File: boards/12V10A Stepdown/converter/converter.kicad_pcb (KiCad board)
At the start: 4 copper layers, 64 x 48 mm, 31 parts, among them J1 TB005-762-02BE, J2 TB005-762-02BE, M1 CSD17578Q3A, M2 CSD17571Q2, U1 LM25145RGYR

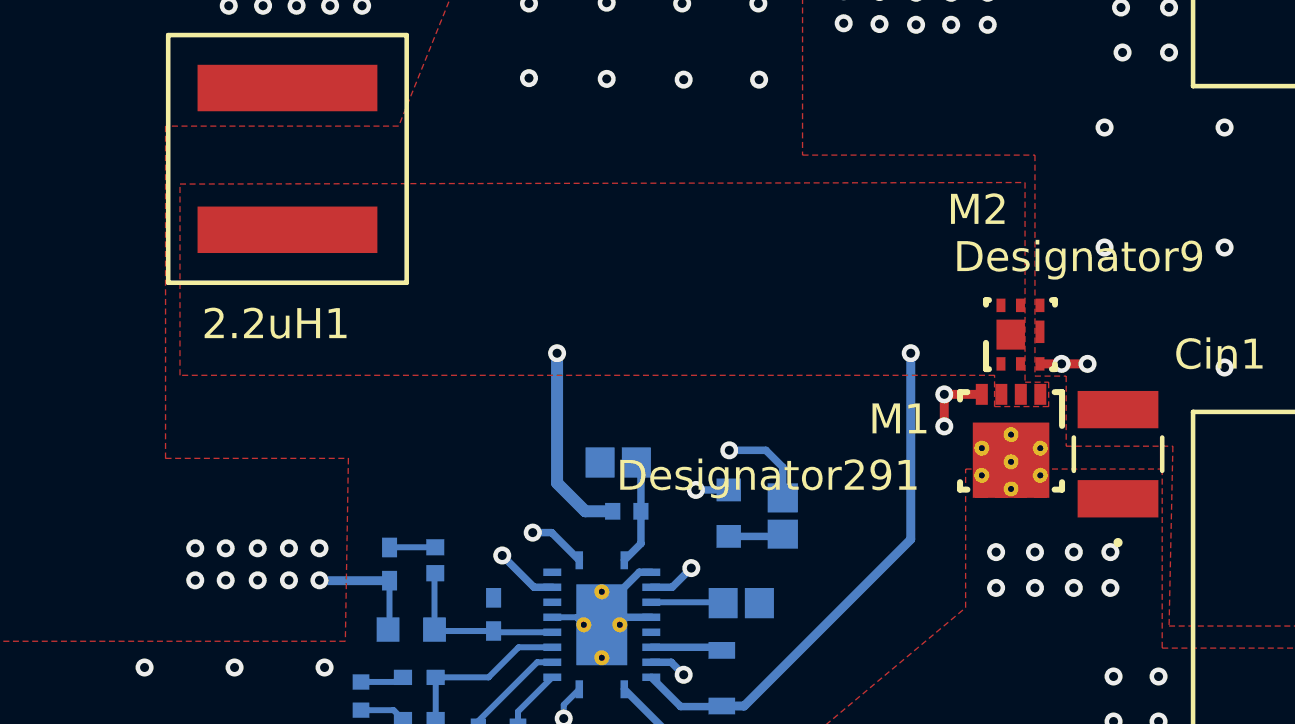
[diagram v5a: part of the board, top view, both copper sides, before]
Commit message: removed backfill on 20a
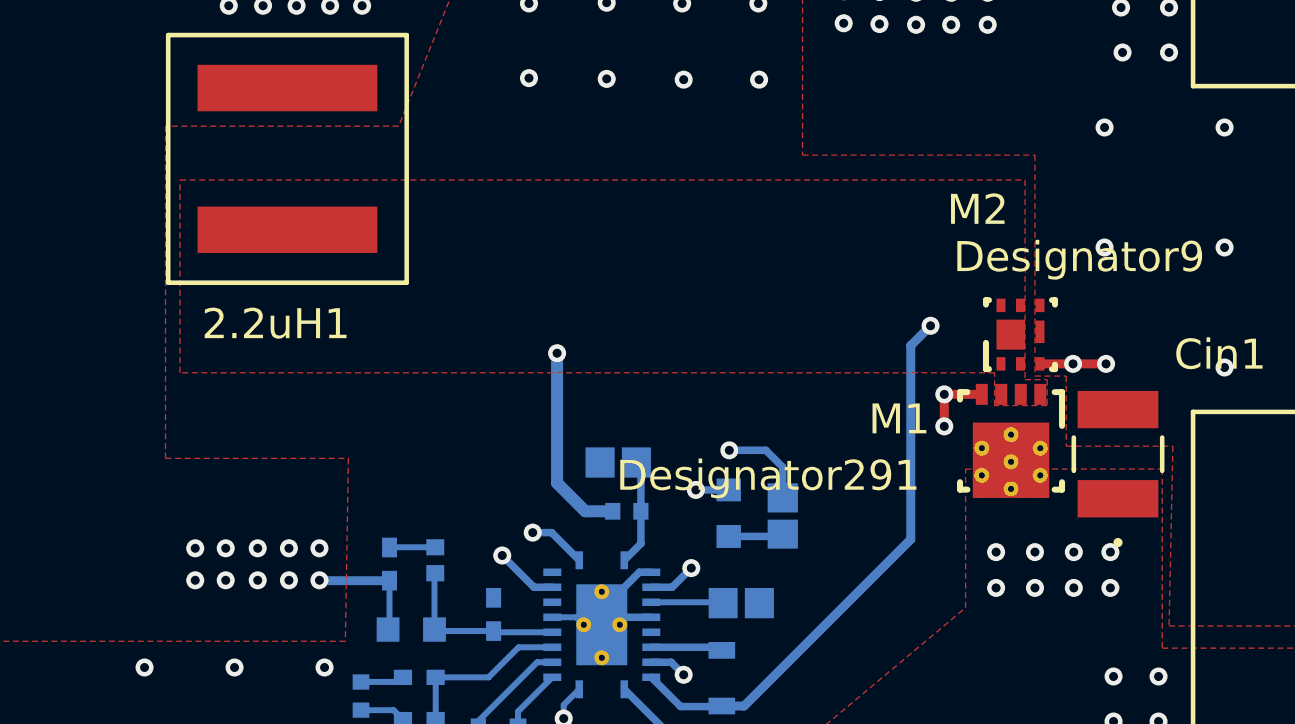
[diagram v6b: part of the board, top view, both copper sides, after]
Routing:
- net Net-(M1-S1): track 24.1 -> 25.3 mm
- net Net-(U1-LO): track 26.1 -> 27.3 mm
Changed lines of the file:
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@@
 	)
 	(via
-		(at 129.54 128.524)
-		(size 0.6)
-		(drill 0.3)
-		(layers "F.Cu" "B.Cu")
+		(at 130.2004 127.6096)
+		(size 0.6)
+		(drill 0.3)
+		(layers "F.Cu" "B.Cu")
+		(net 2)
+	)
+	(segment
+		(start 129.54 134.7295)
+		(end 123.9853 140.2842)
+		(width 0.3)
+		(layer "B.Cu")
+		(net 2)
+	)
+	(segment
+		(start 129.54 128.27)
+		(end 129.54 134.7295)
+		(width 0.3)
+		(layer "B.Cu")
 		(net 2)
 	)
@@
 		(end 123.2408 140.302198)
 		(width 0.25)
-		(layer "B.Cu")
-		(net 2)
-	)
-	(segment
-		(start 129.54 128.524)
-		(end 129.54 134.7295)
-		(width 0.3)
 		(layer "B.Cu")
 		(net 2)
@@
 	)
 	(segment
-		(start 129.54 134.7295)
-		(end 123.9853 140.2842)
-		(width 0.3)
-		(layer "B.Cu")
-		(net 2)
-	)
-	(segment
 		(start 123.9853 140.2842)
 		(end 123.2408 140.2842)
@@
 	)
 	(segment
+		(start 130.2004 127.6096)
+		(end 129.54 128.27)
+		(width 0.3)
+		(layer "B.Cu")
+		(net 2)
+	)
+	(segment
 		(start 123.0346 138.3254)
 		(end 123.2408 138.5316)
@@
 	)
 	(segment
-		(start 134.5692 128.8796)
-		(end 135.4328 128.8796)
+		(start 133.847599 128.8796)
+		(end 134.95 128.8796)
 		(width 0.3)
 		(layer "F.Cu")
@@
 	)
 	(segment
-		(start 133.847599 128.8796)
-		(end 134.5692 128.8796)
+		(start 134.95 128.8796)
+		(end 136.05 128.8796)
 		(width 0.3)
 		(layer "F.Cu")
@@
 	)
 	(via
-		(at 134.5692 128.8796)
+		(at 134.95 128.8796)
 		(size 0.6)
 		(drill 0.3)
@@
 	)
 	(via
-		(at 135.4328 128.8796)
+		(at 136.05 128.8796)
 		(size 0.6)
 		(drill 0.3)
@@
 	)
 	(segment
-		(start 134.0104 125.984)
+		(start 129.9972 125.984)
+		(end 127.8128 128.1684)
+		(width 0.3)
+		(layer "In2.Cu")
+		(net 15)
+	)
+	(segment
+		(start 136 127.45)
+		(end 134.534 125.984)
+		(width 0.3)
+		(layer "In2.Cu")
+		(net 15)
+	)
+	(segment
+		(start 136.05 128.8796)
+		(end 136 128.8296)
+		(width 0.3)
+		(layer "In2.Cu")
+		(net 15)
+	)
+	(segment
+		(start 127.8128 134.4168)
+		(end 126.5428 135.6868)
+		(width 0.3)
+		(layer "In2.Cu")
+		(net 15)
+	)
+	(segment
+		(start 134.534 125.984)
 		(end 129.9972 125.984)
+		(width 0.3)
+		(layer "In2.Cu")
+		(net 15)
+	)
+	(segment
+		(start 136 128.8296)
+		(end 136 127.45)
+		(width 0.3)
+		(layer "In2.Cu")
+		(net 15)
+	)
+	(segment
+		(start 127.8128 128.1684)
+		(end 127.8128 134.4168)
 		(width 0.3)
 		(layer "In2.Cu")
@@
 		(start 126.5428 135.6868)
 		(end 122.2248 135.6868)
-		(width 0.3)
-		(layer "In2.Cu")
-		(net 15)
-	)
-	(segment
-		(start 135.4328 127.4064)
-		(end 134.0104 125.984)
-		(width 0.3)
-		(layer "In2.Cu")
-		(net 15)
-	)
-	(segment
-		(start 129.9972 125.984)
-		(end 128.524 127.4572)
-		(width 0.3)
-		(layer "In2.Cu")
-		(net 15)
-	)
-	(segment
-		(start 128.524 133.7056)
-		(end 126.5428 135.6868)
-		(width 0.3)
-		(layer "In2.Cu")
-		(net 15)
-	)
-	(segment
-		(start 135.4328 128.8796)
-		(end 135.4328 127.4064)
-		(width 0.3)
-		(layer "In2.Cu")
-		(net 15)
-	)
-	(segment
-		(start 128.524 127.4572)
-		(end 128.524 133.7056)
 		(width 0.3)
 		(layer "In2.Cu")
@@
 		(polygon
 			(pts
-				(xy 105.1814 122.8852) (xy 133.35 122.8344) (xy 133.35 129.4892) (xy 134.1374 129.4892) (xy 134.1374 130.302)
-				(xy 132.334 130.302) (xy 132.334 129.2606) (xy 105.1814 129.2606)
+				(xy 105.1814 122.75) (xy 133.35 122.75) (xy 133.35 129.4048) (xy 134.0874 129.4048) (xy 134.0874 130.2676)
+				(xy 132.334 130.2676) (xy 132.334 129.1762) (xy 105.1814 129.1762)
 			)
 		)

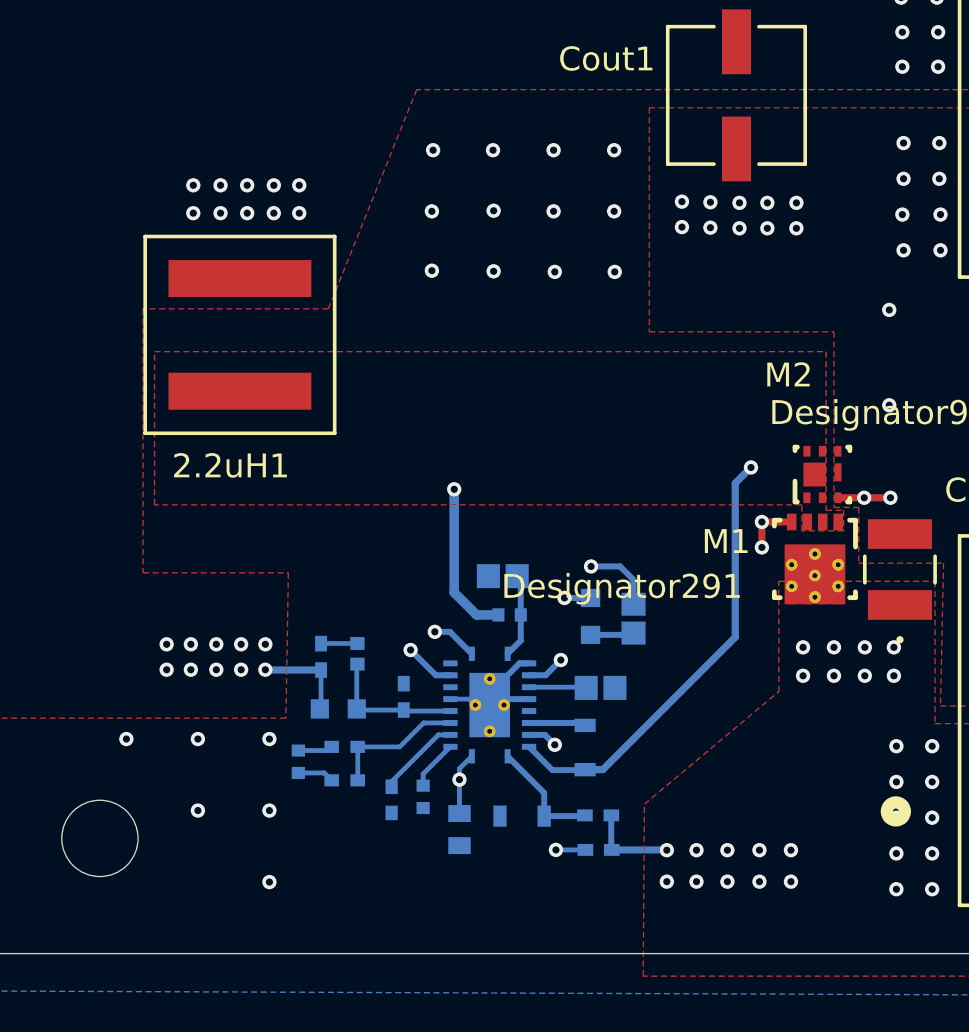
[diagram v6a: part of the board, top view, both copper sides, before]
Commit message: finished fill zones, silkscreens for 10a and restored component rule areas for 20a
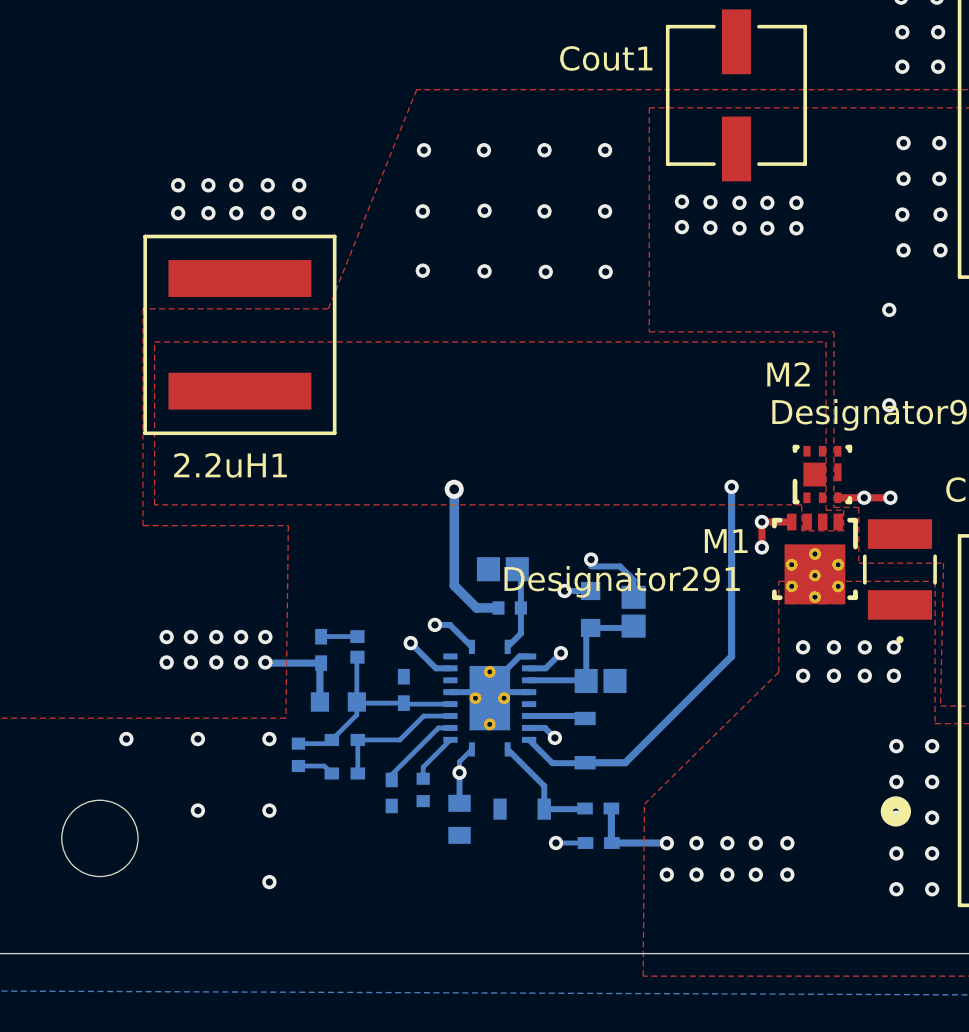
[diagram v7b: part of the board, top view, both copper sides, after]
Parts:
- moved Ruv2 0.43 mm to (118.0, 142.4)
- moved Cbst1 0.29 mm to (123.2, 139.1)
- moved Ccomp1 0.29 mm to (113.2, 140.4)
- moved Ccomp3 0.29 mm to (113.7, 135.1)
- moved Cilim1 0.29 mm to (119.8, 131.9)
- moved Cvin1 0.29 mm to (120.6, 141.9)
- moved Rcomp1 0.29 mm to (111.2, 139.7)
- moved Rcomp2 0.29 mm to (112.2, 135.3)
- moved Rilim1 0.29 mm to (120.1, 133.5)
- moved Rpgood1 0.29 mm to (123.5, 133.6)
- moved Rt1 0.29 mm to (116.5, 141.1)
- moved Rvin1 0.29 mm to (123.8, 141.9)
- moved U1 0.29 mm to (119.2, 137.3)
- moved Css1 0.29 mm to (115.1, 141.3)
- moved Cvcc1 0.29 mm to (123.9, 136.6)
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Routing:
- net Net-(U1-VCC): track 4.41 -> 6.51 mm
- net Net-(U1-FB): track 7.48 -> 9.41 mm
- net Net-(M1-S1): track 25.3 -> 24.1 mm
- net GND: track 5.57 -> 6.17 mm
- net Net-(U1-LO): track 27.3 -> 26.8 mm
- net Net-(M1-G): track 18.2 -> 18.7 mm
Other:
- board text added: "Electrical leads:"
- board text added: "Hriday, Janine"
- board text added: "Members:"
- board text added: "Nathan, Ozan, Irmak, Aadarsh, Abhinav, Josh"

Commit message: moved SW trace
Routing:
- net Net-(M1-S1): track 24.1 -> 23.1 mm
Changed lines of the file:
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@@
 			(outputformat 1)
 			(mirror no)
-			(drillshape 1)
+			(drillshape 0)
 			(scaleselection 1)
-			(outputdirectory "")
+			(outputdirectory "Manufacturing/")
 		)
 	)
@@
 	)
 	(via
-		(at 129.3876 128.4224)
+		(at 126.6952 128.3208)
 		(size 0.6)
 		(drill 0.3)
@@
 	)
 	(segment
-		(start 129.3876 135.5344)
-		(end 124.928199 139.993801)
-		(width 0.3)
-		(layer "B.Cu")
-		(net 2)
-	)
-	(segment
 		(start 121.870795 140.011799)
 		(end 123.243798 140.011799)
@@
 	)
 	(segment
-		(start 129.3876 128.4224)
-		(end 129.3876 135.5344)
+		(start 124.928199 139.993801)
+		(end 123.243798 139.993801)
 		(width 0.3)
 		(layer "B.Cu")
@@
 	)
 	(segment
-		(start 124.928199 139.993801)
-		(end 123.243798 139.993801)
+		(start 126.6952 128.3208)
+		(end 126.6952 138.2268)
+		(width 0.3)
+		(layer "B.Cu")
+		(net 2)
+	)
+	(segment
+		(start 126.6952 138.2268)
+		(end 124.928199 139.993801)
 		(width 0.3)
 		(layer "B.Cu")
@@
 	)
 	(segment
-		(start 136 128.8296)
-		(end 136 127.45)
+		(start 134.534 125.984)
+		(end 129.9972 125.984)
 		(width 0.3)
 		(layer "In2.Cu")
@@
 	)
 	(segment
-		(start 129.9972 125.984)
-		(end 127.8128 128.1684)
+		(start 127.9652 133.5532)
+		(end 126.121999 135.396401)
 		(width 0.3)
 		(layer "In2.Cu")
@@
 	)
 	(segment
-		(start 136 127.45)
-		(end 134.534 125.984)
+		(start 126.121999 135.396401)
+		(end 122.227798 135.396401)
 		(width 0.3)
 		(layer "In2.Cu")
@@
 	)
 	(segment
-		(start 126.121999 135.396401)
-		(end 122.227798 135.396401)
+		(start 129.9972 125.984)
+		(end 127.9652 128.016)
 		(width 0.3)
 		(layer "In2.Cu")
@@
 	)
 	(segment
-		(start 134.534 125.984)
-		(end 129.9972 125.984)
+		(start 136.05 128.8796)
+		(end 136 128.8296)
 		(width 0.3)
 		(layer "In2.Cu")
@@
 	)
 	(segment
-		(start 136.05 128.8796)
-		(end 136 128.8296)
+		(start 136 128.8296)
+		(end 136 127.45)
 		(width 0.3)
 		(layer "In2.Cu")
@@
 	)
 	(segment
-		(start 127.8128 133.7056)
-		(end 126.121999 135.396401)
+		(start 136 127.45)
+		(end 134.534 125.984)
 		(width 0.3)
 		(layer "In2.Cu")
@@
 	)
 	(segment
-		(start 127.8128 128.1684)
-		(end 127.8128 133.7056)
+		(start 127.9652 128.016)
+		(end 127.9652 133.5532)
 		(width 0.3)
 		(layer "In2.Cu")
@@
 	)
 	(via
-		(at 123.4948 131.4704)
+		(at 123.330997 131.4704)
 		(size 0.6)
 		(drill 0.3)
@@
 	)
 	(segment
-		(start 125.2746 133.346599)
-		(end 125.2746 132.324397)
+		(start 125.2746 132.324397)
+		(end 125.2746 133.346599)
 		(width 0.25)
 		(layer "B.Cu")
@@
 	)
 	(segment
-		(start 123.491802 131.760799)
-		(end 124.711002 131.760799)
+		(start 116.985 136.035)
+		(end 117.594 136.035)
 		(width 0.25)
 		(layer "B.Cu")
@@
 	)
 	(segment
-		(start 116.985 136.035)
-		(end 117.594 136.035)
+		(start 123.330997 131.4704)
+		(end 123.621397 131.760799)
 		(width 0.25)
 		(layer "B.Cu")
@@
 	)
 	(segment
-		(start 117.681198 129.960801)
-		(end 121.821398 129.960801)
+		(start 123.621397 131.760799)
+		(end 124.711002 131.760799)
 		(width 0.25)
-		(layer "In2.Cu")
+		(layer "B.Cu")
 		(net 19)
 	)
 	(segment
-		(start 123.327999 131.760799)
-		(end 123.491802 131.760799)
+		(start 117.681198 129.960801)
+		(end 121.821398 129.960801)
 		(width 0.25)
 		(layer "In2.Cu")
